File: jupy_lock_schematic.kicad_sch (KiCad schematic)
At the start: 21 parts, among them J1 PWR, J10 FPR, J11 PIR, J2 LOCK, J3 OPEN_BTN, J4 BELL_BTN, J5 ILI9341_DISP, J6 UART_COMM, J7 K230D_PWR, J8 PWR_2, J9 Barrel_Jack_MountingPin, Q1 BUZ11, Q2 BUZ11, U1 PTN78060W_EUW-7, U2 ESP32-C5-DevKitC-1

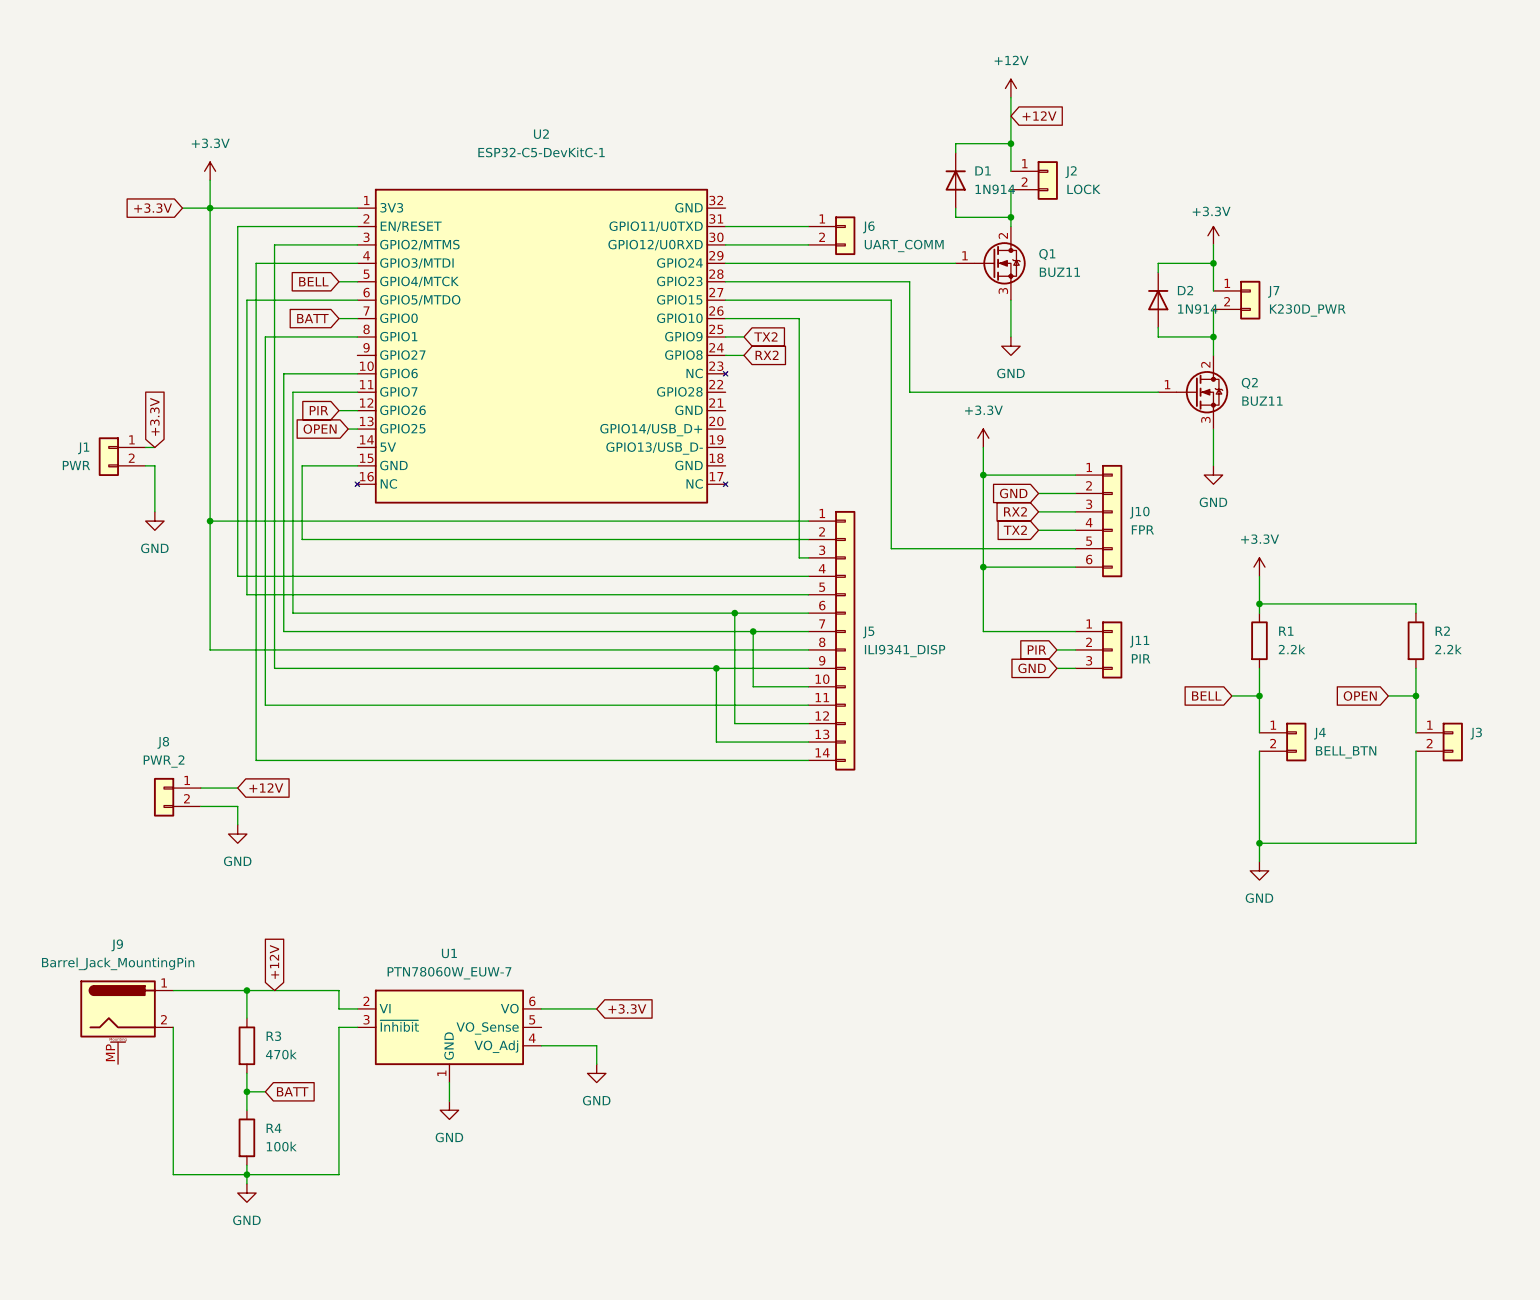
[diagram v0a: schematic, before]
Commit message: Refactor code structure for improved readability and maintainability - Lots of edits done will need to come back and seperate and re commit
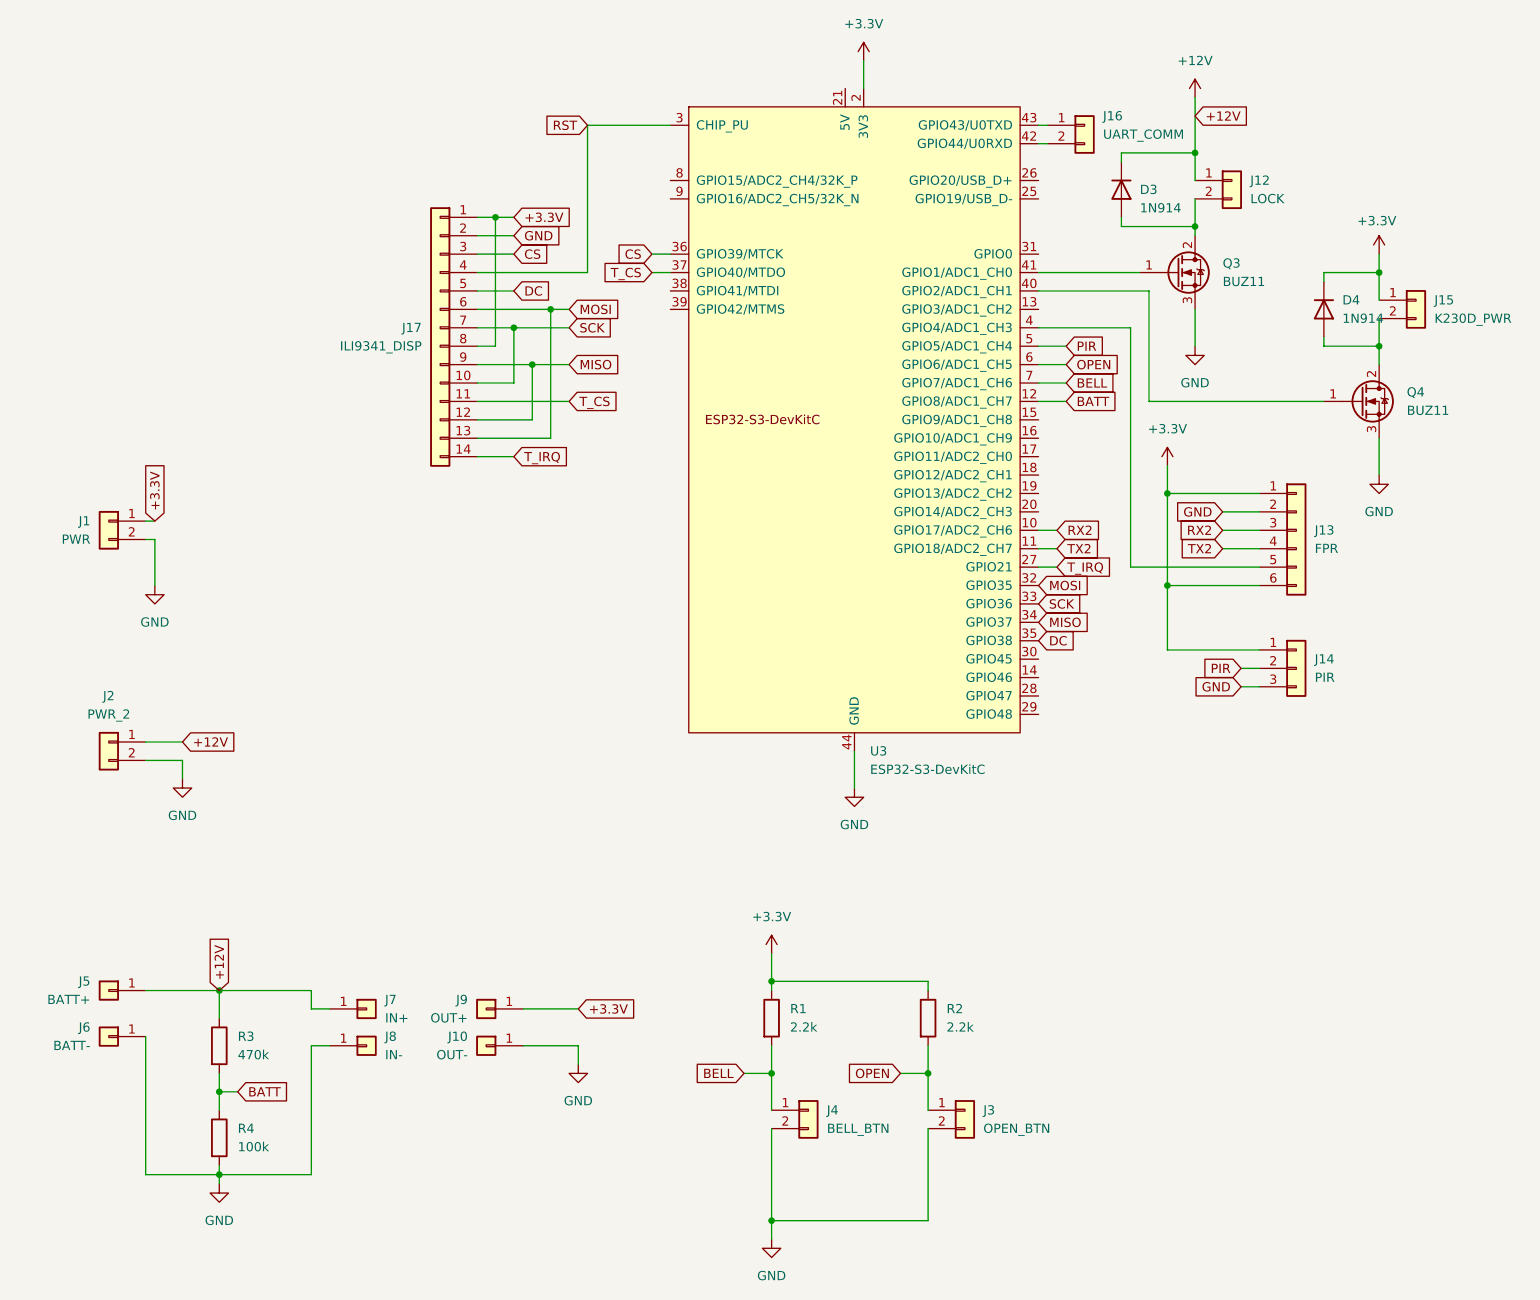
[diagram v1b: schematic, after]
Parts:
- removed D1, D2: 1N914, Diode_SMD:D_SOD-523, symbol Diode:1N914
- removed J10: FPR, Connector_JST:JST_EH_B6B-EH-A_1x06_P2.50mm_Vertical, symbol Connector_Generic:Conn_01x06
- removed J11: PIR, Connector_JST:JST_EH_B3B-EH-A_1x03_P2.50mm_Vertical, symbol Connector_Generic:Conn_01x03
- removed J5: ILI9341_DISP, Connector_JST:JST_EH_B14B-EH-A_1x14_P2.50mm_Vertical, symbol Connector_Generic:Conn_01x14
- removed J6: UART_COMM, Connector_JST:JST_EH_B2B-EH-A_1x02_P2.50mm_Vertical, symbol Connector_Generic:Conn_01x02
- removed J7: K230D_PWR, Connector_JST:JST_EH_B2B-EH-A_1x02_P2.50mm_Vertical, symbol Connector_Generic:Conn_01x02
- removed J8: PWR_2, Connector_JST:JST_EH_B2B-EH-A_1x02_P2.50mm_Vertical, symbol Connector_Generic:Conn_01x02
- removed J9: Barrel_Jack_MountingPin, Connector_BarrelJack:BarrelJack_Horizontal, symbol Connector:Barrel_Jack_MountingPin
- removed Q1, Q2: BUZ11, Package_TO_SOT_THT:TO-220-3_Vertical, symbol Transistor_FET:BUZ11
- removed U1: PTN78060W_EUW-7, Module:Texas_EUW_R-PDSS-T7_THT, symbol Converter_DCDC:PTN78060W_EUW-7
- removed U2: ESP32-C5-DevKitC-1, PCM_Espressif:ESP32-C6-WROOM-1, symbol PCM_Espressif:ESP32-C5-DevKitC-1
- added D3, D4: 1N914, Diode_SMD:D_SOD-523, symbol Diode:1N914
- added J10: OUT-, symbol Connector_Generic:Conn_01x01
- added J12: LOCK, Connector_JST:JST_EH_B2B-EH-A_1x02_P2.50mm_Vertical, symbol Connector_Generic:Conn_01x02
- added J13: FPR, Connector_JST:JST_EH_B6B-EH-A_1x06_P2.50mm_Vertical, symbol Connector_Generic:Conn_01x06
- added J14: PIR, Connector_JST:JST_EH_B3B-EH-A_1x03_P2.50mm_Vertical, symbol Connector_Generic:Conn_01x03
- added J15: K230D_PWR, Connector_JST:JST_EH_B2B-EH-A_1x02_P2.50mm_Vertical, symbol Connector_Generic:Conn_01x02
- added J16: UART_COMM, Connector_JST:JST_EH_B2B-EH-A_1x02_P2.50mm_Vertical, symbol Connector_Generic:Conn_01x02
- added J17: ILI9341_DISP, Connector_JST:JST_EH_B14B-EH-A_1x14_P2.50mm_Vertical, symbol Connector_Generic:Conn_01x14
- added J5: BATT+, symbol Connector_Generic:Conn_01x01
- added J6: BATT-, symbol Connector_Generic:Conn_01x01
- added J7: IN+, symbol Connector_Generic:Conn_01x01
- added J8: IN-, symbol Connector_Generic:Conn_01x01
- added J9: OUT+, symbol Connector_Generic:Conn_01x01
- added Q3, Q4: BUZ11, Package_TO_SOT_THT:TO-220-3_Vertical, symbol Transistor_FET:BUZ11
- added U3: ESP32-S3-DevKitC, PCM_Espressif:ESP32-S3-DevKitC, symbol PCM_Espressif:ESP32-S3-DevKitC
- J2: value LOCK -> PWR_2
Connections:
- net +12V: now also D3.1 (K), J12.1 (Pin_1), J5.1 (Pin_1), J7.1 (Pin_1)
- net +3.3V: now also D4.1 (K), J13.1 (Pin_1), J13.6 (Pin_6), J14.1 (Pin_1), J15.1 (Pin_1), J17.1 (Pin_1), J17.8 (Pin_8), J9.1 (Pin_1), U3.1 (3V3), U3.2 (3V3)
- net BATT: now also U3.12 (GPIO8/ADC1_CH7)
- net BELL: now also U3.7 (GPIO7/ADC1_CH6)
- net GND: now also J2.2 (Pin_2), J10.1 (Pin_1), J13.2 (Pin_2), J14.3 (Pin_3), J17.2 (Pin_2), J6.1 (Pin_1), J8.1 (Pin_1), Q3.3 (S), Q4.3 (S), U3.22 (GND), U3.23 (GND), U3.24 (GND), U3.44 (GND)
- net OPEN: now also U3.6 (GPIO6/ADC1_CH5)
- net PIR: now also J14.2 (Pin_2), U3.5 (GPIO5/ADC1_CH4)
- net RX2: now also J13.3 (Pin_3), U3.10 (GPIO17/ADC2_CH6)
- net TX2: now also J13.4 (Pin_4), U3.11 (GPIO18/ADC2_CH7)
- new net: D3.2 (A), J12.2 (Pin_2), Q3.2 (D)
- new net: Q3.1 (G), U3.41 (GPIO1/ADC1_CH0)
- new net: D4.2 (A), J15.2 (Pin_2), Q4.2 (D)
- new net: J13.5 (Pin_5), U3.4 (GPIO4/ADC1_CH3)
- new net: Q4.1 (G), U3.40 (GPIO2/ADC1_CH1)
- new net: J16.2 (Pin_2), U3.42 (GPIO44/U0RXD)
- new net: J16.1 (Pin_1), U3.43 (GPIO43/U0TXD)
- new net CS: J17.3 (Pin_3), U3.36 (GPIO39/MTCK)
- new net DC: J17.5 (Pin_5), U3.35 (GPIO38)
- new net MISO: J17.12 (Pin_12), J17.9 (Pin_9), U3.34 (GPIO37)
- new net MOSI: J17.13 (Pin_13), J17.6 (Pin_6), U3.32 (GPIO35)
- new net RST: J17.4 (Pin_4), U3.3 (CHIP_PU)
- new net SCK: J17.10 (Pin_10), J17.7 (Pin_7), U3.33 (GPIO36)
- new net T_CS: J17.11 (Pin_11), U3.37 (GPIO40/MTDO)
- new net T_IRQ: J17.14 (Pin_14), U3.27 (GPIO21)
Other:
- title: (none) -> Smart Lock Board
- moved on the sheet: J1, J3, J4, R1, R2, R3, R4
